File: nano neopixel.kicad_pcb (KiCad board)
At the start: 2 copper layers, 35.5 x 48.2 mm, 13 parts

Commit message: added 470ohm signal series resistors, and 1000uF tank cap on Vin
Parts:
- added JP1: Jumper_Open, Jumper:SolderJumper-2_P1.3mm_Open_Pad1.0x1.5mm, F.Cu at (108.3, 75.8)
- added JP2: Jumper_Open, Jumper:SolderJumper-2_P1.3mm_Open_Pad1.0x1.5mm, F.Cu at (108.0, 79.9)
- added JP3: Jumper_Open, Jumper:SolderJumper-2_P1.3mm_Open_Pad1.0x1.5mm, F.Cu at (107.8, 84.1)
- added JP4: Jumper_Open, Jumper:SolderJumper-2_P1.3mm_Open_Pad1.0x1.5mm, F.Cu at (107.5, 88.1)
- added JP5: Jumper_Open, Jumper:SolderJumper-2_P1.3mm_Open_Pad1.0x1.5mm, F.Cu at (107.4, 92.3)
- added JP6: Jumper_Open, Jumper:SolderJumper-2_P1.3mm_Open_Pad1.0x1.5mm, F.Cu at (107.3, 96.9)
- added R1: 470, Resistor_SMD:R_0805_2012Metric, F.Cu at (95.2, 73.6)
- added R2: 470, Resistor_SMD:R_0805_2012Metric, F.Cu at (95.1, 77.0)
- added R3: 470, Resistor_SMD:R_0805_2012Metric, F.Cu at (94.6, 80.7)
- added R4: 470, Resistor_SMD:R_0805_2012Metric, F.Cu at (94.8, 84.7)
- added R5: 470, Resistor_SMD:R_0805_2012Metric, F.Cu at (94.0, 88.5)
- added R6: 470, Resistor_SMD:R_0805_2012Metric, F.Cu at (93.8, 91.6)
- A1: renamed from ARDUINO NANO
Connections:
- D2 pad 3: STRIP1 -> Net-(D2-Pad3)
- D3 pad 3: STRIP2 -> Net-(D3-Pad3)
- D4 pad 3: STRIP3 -> Net-(D4-Pad3)
- D5 pad 3: STRIP4 -> Net-(D5-Pad3)
- D6 pad 3: STRIP5 -> Net-(D6-Pad3)
- D7 pad 3: STRIP6 -> Net-(D7-Pad3)
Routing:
- net STRIP6: track 3.87 -> 0.00 mm
- net Net-(D7-Pad3): track 0.00 -> 3.87 mm
- net STRIP2: track 3.86 -> 0.00 mm
- net Net-(D3-Pad3): track 0.00 -> 3.86 mm
- net STRIP5: track 3.76 -> 0.00 mm
- net Net-(D6-Pad3): track 0.00 -> 3.76 mm
- net STRIP3: track 3.54 -> 0.00 mm
- net Net-(D4-Pad3): track 0.00 -> 3.54 mm

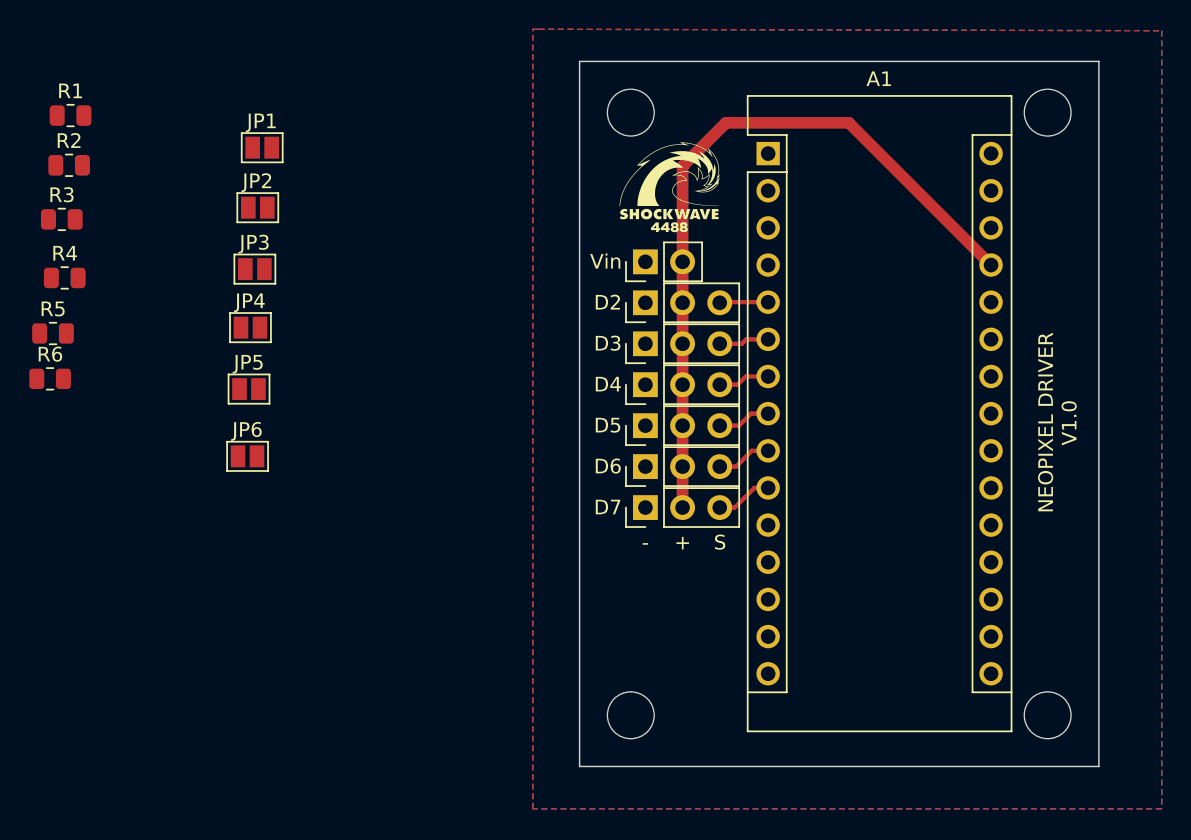
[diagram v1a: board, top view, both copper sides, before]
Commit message: added 2 more DIO connections, routed all traces
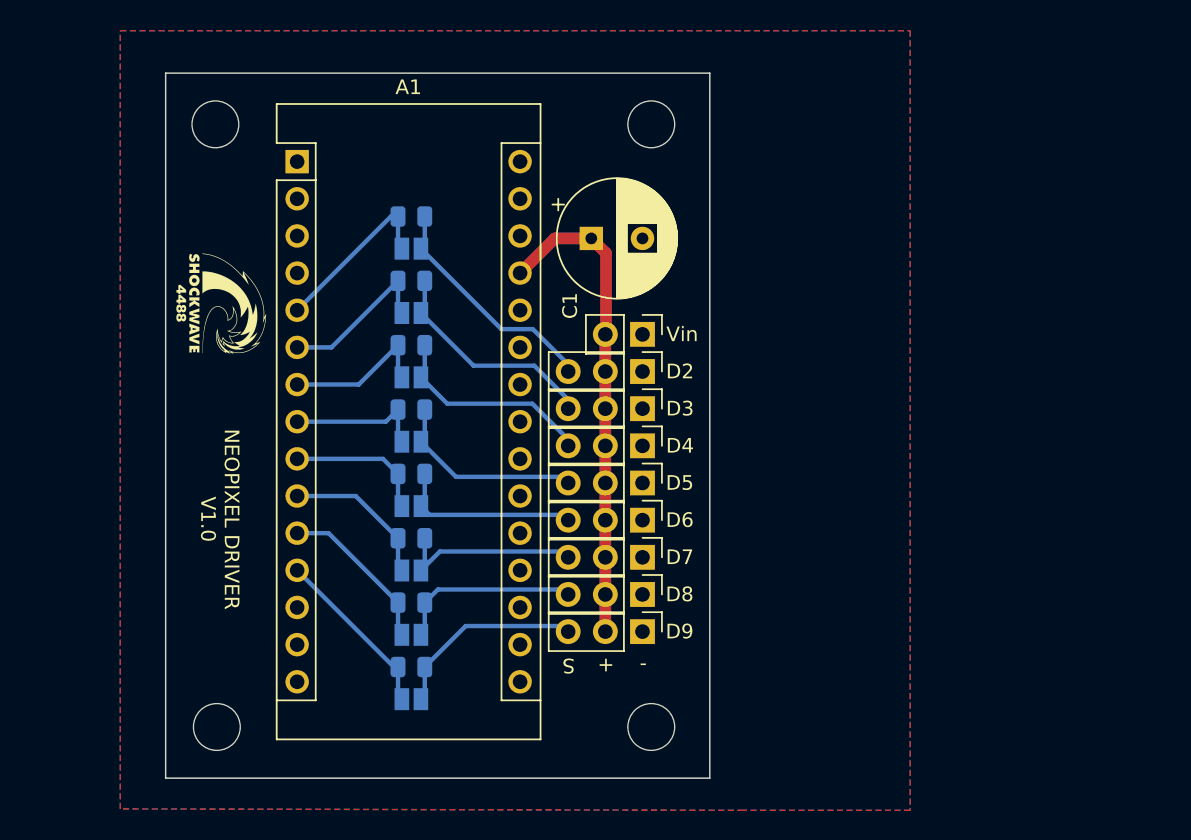
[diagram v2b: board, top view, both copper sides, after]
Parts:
- added C1: 1000u, Capacitor_THT:CP_Radial_D8.0mm_P3.50mm, F.Cu at (130.8, 82.0)
- added D8: Conn_01x03, Connector_PinHeader_2.54mm:PinHeader_1x03_P2.54mm_Vertical, F.Cu at (134.3, 106.3)
- added D9: Conn_01x03, Connector_PinHeader_2.54mm:PinHeader_1x03_P2.54mm_Vertical, F.Cu at (134.3, 108.9)
- added JP7: Jumper_Open, Jumper:SolderJumper-2_P1.3mm_Open_Pad1.0x1.5mm, B.Cu at (118.5, 109.1)
- added JP8: Jumper_Open, Jumper:SolderJumper-2_P1.3mm_Open_Pad1.0x1.5mm, B.Cu at (118.5, 113.5)
- added R7: 470, Resistor_SMD:R_0805_2012Metric, B.Cu at (118.5, 106.9)
- added R8: 470, Resistor_SMD:R_0805_2012Metric, B.Cu at (118.5, 111.3)
- JP1, JP2, JP3, JP4, JP5, JP6, R1, R2, R3, R4, R5, R6: moved to B.Cu
- moved H3 70.6 mm to (105.2, 115.4), turned to 180 degrees
- moved H4 69.6 mm to (105.2, 74.2), turned to 180 degrees
- moved H2 42.0 mm to (134.9, 115.4), turned to 180 degrees
- moved H1 40.4 mm to (134.9, 74.2), turned to 180 degrees
- moved A1 32.2 mm to (110.7, 76.8)
- moved G*** 31.6 mm to (105.5, 86.4), turned to -90 degrees
- moved R6 27.0 mm to (118.5, 102.5)
- moved R5 26.3 mm to (118.5, 98.1)
- moved R3 25.4 mm to (118.5, 89.3)
- moved R4 25.4 mm to (118.5, 93.7)
- moved R2 24.7 mm to (118.5, 84.9)
- moved R1 24.3 mm to (118.5, 80.5)
- moved JP5 13.7 mm to (118.5, 100.3)
- moved JP6 13.6 mm to (118.5, 104.7)
- moved JP4 13.5 mm to (118.5, 95.9)
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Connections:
- net STRIP1 renamed D2
- net STRIP2 renamed D3
- net STRIP3 renamed D4
- net STRIP4 renamed D5
- net STRIP5 renamed D6
- net STRIP6 renamed D7
- A1 pad 11: unconnected-(A1-Pad11) -> D8
- A1 pad 12: unconnected-(A1-Pad12) -> D9
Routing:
- net +5V: track 49.7 -> 33.3 mm
- net Net-(D2-Pad3): track 0.00 -> 16.1 mm
- net Net-(D5-Pad3): track 0.00 -> 13.7 mm
- net Net-(D9-Pad3): track 0.00 -> 13.4 mm
- net Net-(D8-Pad3): track 0.00 -> 12.6 mm
- net D9: track 0.00 -> 11.9 mm
- net Net-(D3-Pad3): track 3.86 -> 15.5 mm
- net D8: track 0.00 -> 11.2 mm
- net D3: track 0.00 -> 11.1 mm
- net Net-(D4-Pad3): track 3.54 -> 14.6 mm
- net D7: track 0.00 -> 10.4 mm
- net D4: track 0.00 -> 10.3 mm
- net D6: track 0.00 -> 9.63 mm
- net Net-(D7-Pad3): track 3.87 -> 13.1 mm
- net Net-(D6-Pad3): track 3.76 -> 12.8 mm
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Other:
- board size 35.5 x 48.2 mm -> 37.2 x 48.2 mm

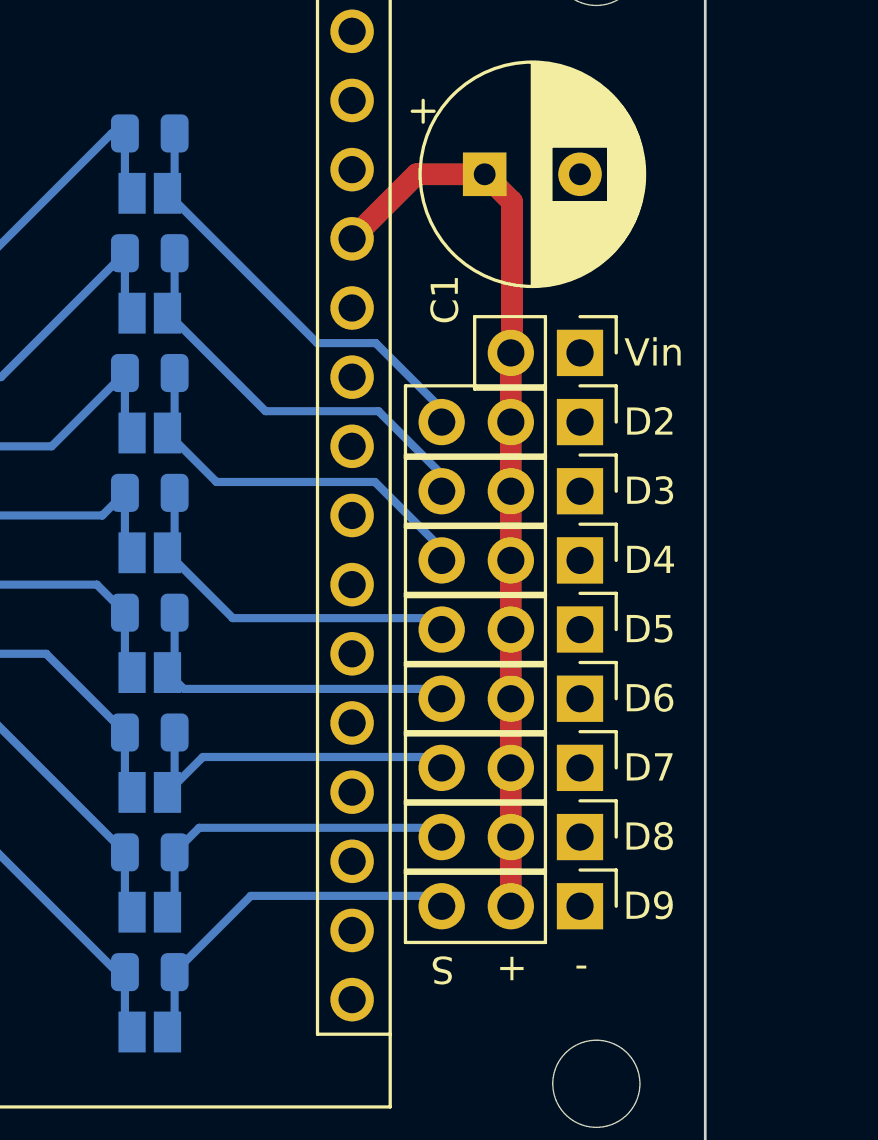
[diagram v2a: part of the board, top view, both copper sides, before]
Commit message: added DIO labels to the resistors and jumpers
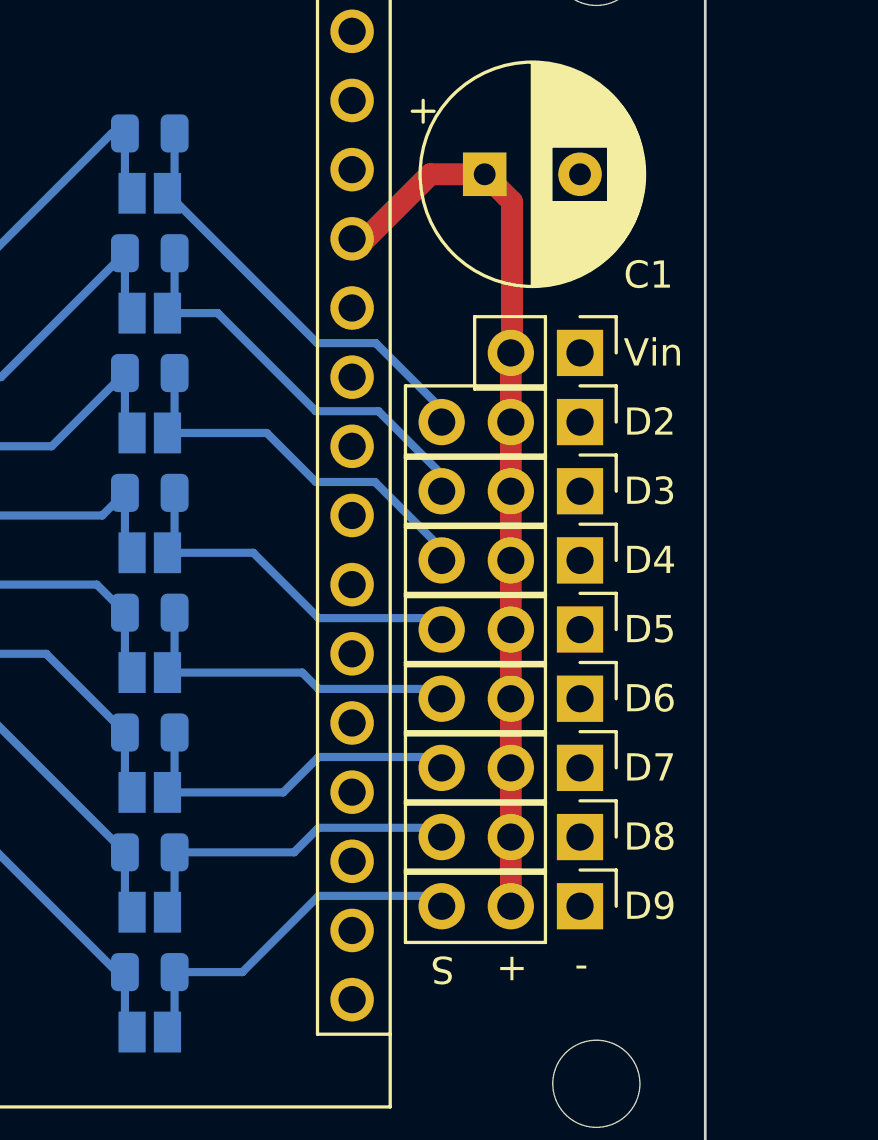
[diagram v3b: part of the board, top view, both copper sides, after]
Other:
- board text added: "D2"
- board text added: "D3"
- board text added: "D4"
- board text added: "D5"
- board text added: "D6"
- board text added: "D7"
- board text added: "D8"
- board text added: "D9"

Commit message: Added JLC tracking number location
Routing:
- net unconnected-(A1-Pad25): track 0.95 -> 0.00 mm
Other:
- board text added: "JLCJLCJLCJLC"
